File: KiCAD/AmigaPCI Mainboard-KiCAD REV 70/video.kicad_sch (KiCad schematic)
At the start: 101 parts, among them CN300 DB15_Female_HighDensity, CN301 Video-Slot, CN302 Video-Slot, J303 HSYNC/COMPSYNC, Q300 MMBT3904, Q301 MMBT3904, Q302 MMBT3904, Q303 MMBT3904, Q304 MMBT3904, Q305 MMBT3906, U300 8362, U301 74AHCT244, U302 74AHCT244, U303 74HCT74, U305 74HCT08

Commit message: Add JLCPCB part numbers and fix 74LVC244 footprints.
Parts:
- C300: LCSC (none) -> C21120
- C301, C304, C312, C315, C316: LCSC (none) -> C14858
- C302, C303, C305, C306, C308, C309, C310, C311, C317: LCSC (none) -> C14663
- C307: LCSC (none) -> C1671
- C313, C314: LCSC (none) -> C59353
- CN300: LCSC (none) -> C379814
- CN301, CN302: LCSC (none) -> C5173302
- FB300, FB301, FB302: LCSC (none) -> C2762183
- J303: LCSC (none) -> C49257
- Q300, Q301, Q302, Q303, Q304: LCSC (none) -> C84104
- Q305: LCSC (none) -> C75549
- R226, R301, R304, R313, R314, R315, R316, R317, R318, R319, R320, R321, R322, R323, R324: LCSC (none) -> C23182
- R300, R305, R308: LCSC (none) -> C25804
- R302: LCSC (none) -> C22936
- R303, R309, R311, R312, R325, R333, R341, R349: LCSC (none) -> C21190
- R307: LCSC (none) -> C23345
- R326, R334, R342: LCSC (none) -> C22975
- R327, R335, R343: LCSC (none) -> C23018
- R328, R336, R363: LCSC (none) -> C25981
- R329, R337, R344: LCSC (none) -> C23179
- R330, R338, R345: LCSC (none) -> C23151
- R331, R332, R339, R340, R346, R347, R352, R362: LCSC (none) -> C4275
- R348: LCSC (none) -> C22962
- R350: LCSC (none) -> C22967
- R351: LCSC (none) -> C22808
- R353, R356: LCSC (none) -> C23033
- R354: LCSC (none) -> C25952
- R355: LCSC (none) -> C25977
- R357: LCSC (none) -> C23265
- R358: LCSC (none) -> C22898
- R359: LCSC (none) -> C22966
- R360: LCSC (none) -> C23154
- R361: LCSC (none) -> C23148
- RN301, RN302: LCSC (none) -> C728819
- U300: LCSC (none) -> C5510465
- U301, U302: LCSC (none) -> C135583
- U303: LCSC (none) -> C141335
- U305: LCSC (none) -> C131488

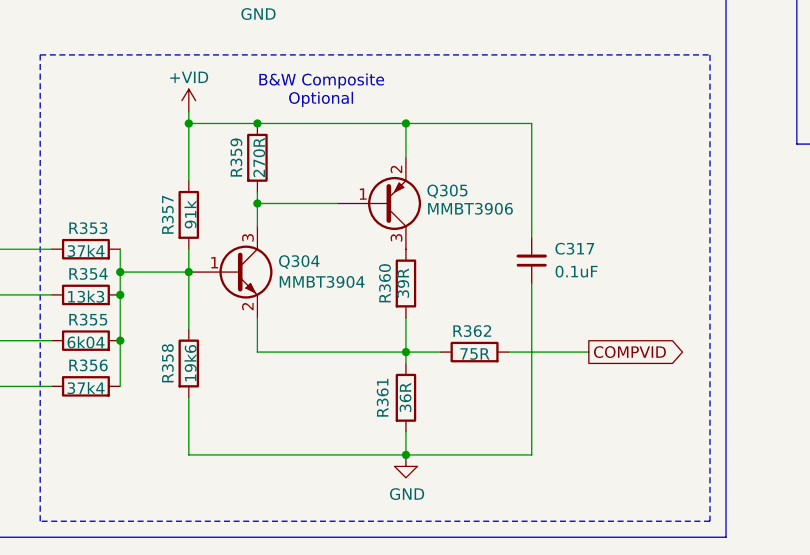
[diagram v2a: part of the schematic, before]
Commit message: Fix value of R360.
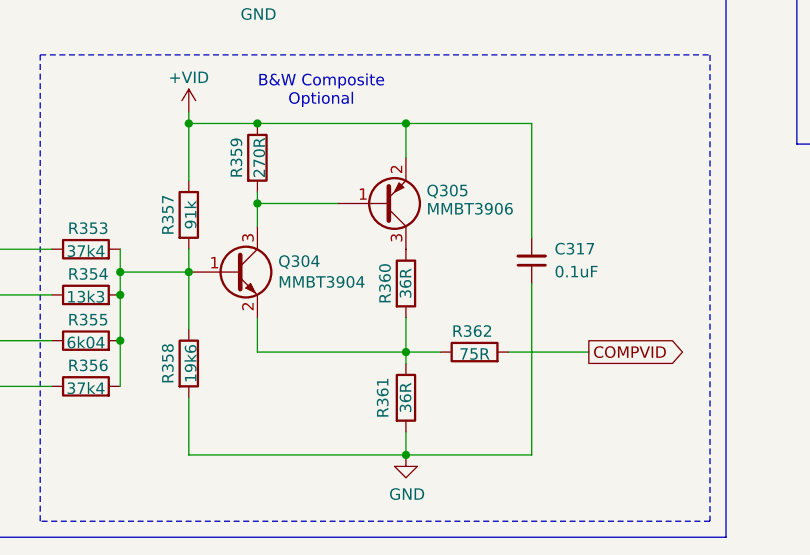
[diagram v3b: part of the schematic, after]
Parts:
- R360: value 39R -> 36R; LCSC C23154 -> C23148
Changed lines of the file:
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@@
 	(title_block
 		(title "AMIGA PCI")
-		(date "2026-04-23")
+		(date "2026-04-27")
 		(rev "7.0")
 	)
@@
 			)
 		)
-		(property "Value" "39R"
-			(at 258.826 237.49 90)
+		(property "Value" "36R"
+			(at 259.08 237.49 90)
 			(effects
 				(font
@@
 			)
 		)
-		(property "LCSC" "C23154"
+		(property "LCSC" "C23148"
 			(at 259.08 237.49 0)
 			(effects

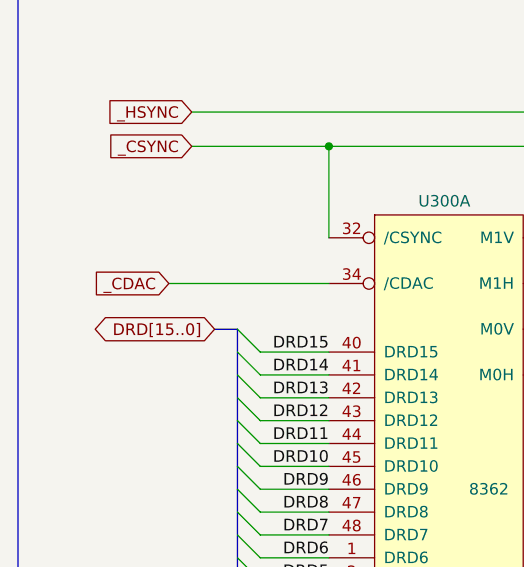
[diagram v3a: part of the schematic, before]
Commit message: Updates to revision 7 board.
Change U810 to 74LVC245 buffers
Add CDAC to U712
Add address latch to CIAs
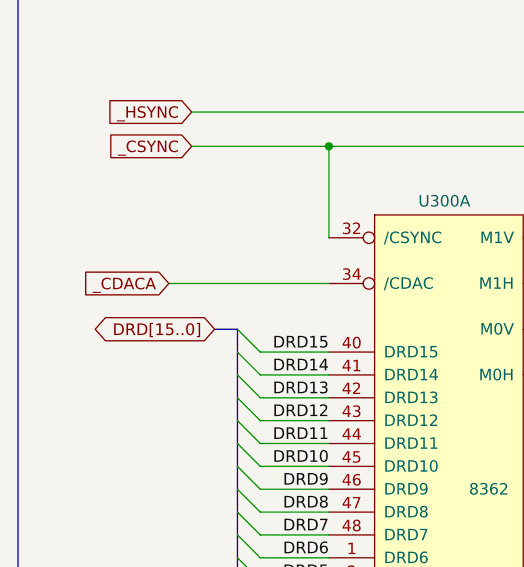
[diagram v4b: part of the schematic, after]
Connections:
- net _CDAC renamed _CDACA
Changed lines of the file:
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@@
 	(title_block
 		(title "AMIGA PCI")
-		(date "2026-04-27")
+		(date "2026-06-06")
 		(rev "7.0")
 	)
@@
 		)
 	)
-	(global_label "_CDAC"
+	(global_label "_CDACA"
 		(shape input)
 		(at 30.48 49.53 180)
@@
 		)
 		(property "Intersheetrefs" "${INTERSHEET_REFS}"
-			(at 21.708 49.53 0)
+			(at 20.54 49.53 0)
 			(effects
 				(font

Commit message: New hardware rev files.
Gerber
BOM w/JLCPCB part numbers
Pick-n-Place File
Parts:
- U301, U302: LCSC C135583 -> C484743
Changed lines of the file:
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@@
 			)
 		)
-		(property "LCSC" "C135583"
+		(property "LCSC" "C484743"
 			(at 135.89 137.16 0)
 			(effects
@@
 			)
 		)
-		(property "LCSC" "C135583"
+		(property "LCSC" "C484743"
 			(at 135.89 60.96 0)
 			(effects
